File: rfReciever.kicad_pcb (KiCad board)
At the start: 4 copper layers, 22.8 x 34 mm, 34 parts, among them J1 MOLEX 1054440001, SW1 RF_RESET, SW2 RF_SLEEP, U1 TLV70130DBVR, U2 USBLC6-2SC6, U3 FT234XD-R, X1 DigiXBeeRX900Micro

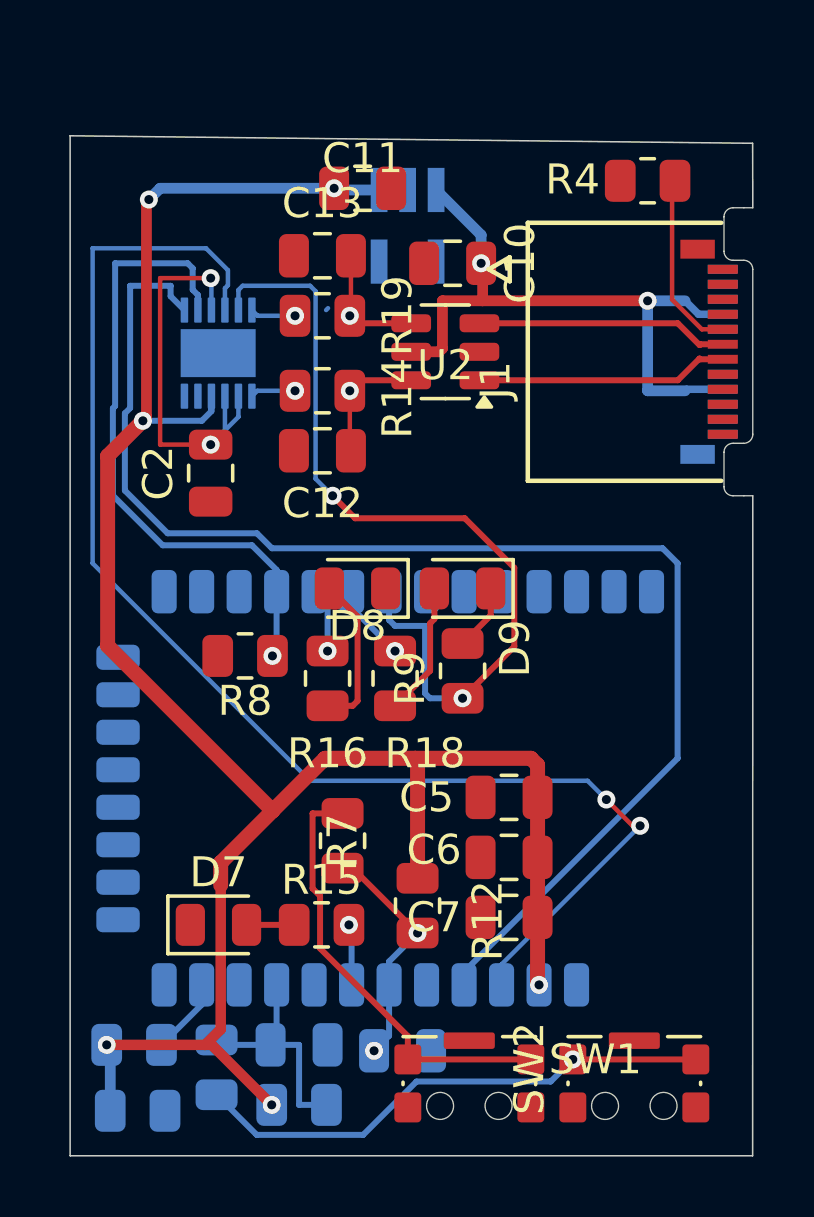
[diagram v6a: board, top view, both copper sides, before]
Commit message: added testpoints, TODO: Ground pours + ground conn
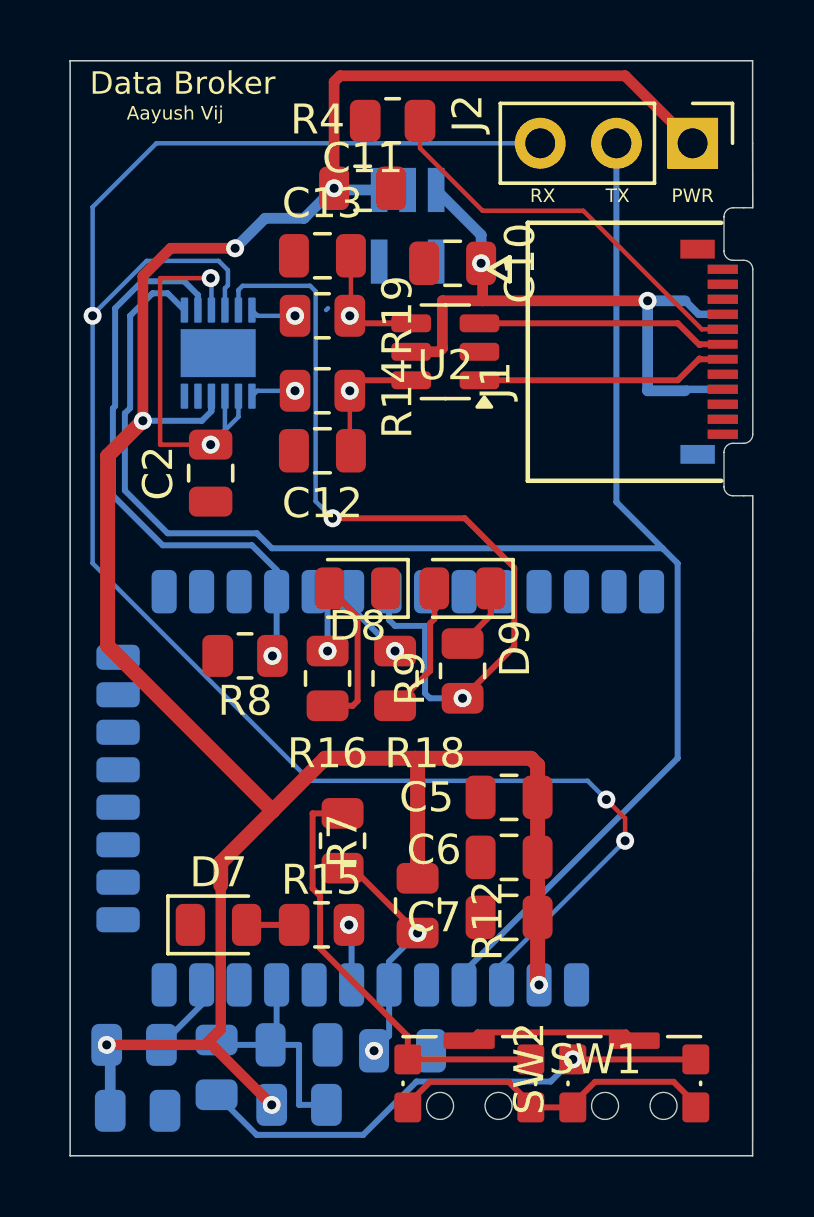
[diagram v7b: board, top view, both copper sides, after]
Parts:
- added J2: Conn_01x03, Connector_PinHeader_2.54mm:PinHeader_1x03_P2.54mm_Vertical, F.Cu at (153.8, 54.5)
- moved R4 8.73 mm to (143.8, 53.8)
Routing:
- net /RF_RXD: track 45.8 -> 63.0 mm, vias 2 -> 3
- net GND: track 2.23 -> 19.2 mm
- net +3.3V: track 72.8 -> 87.9 mm
- net /RF_TXD: track 45.7 -> 58.8 mm
- net Net-(J1-CC): track 6.46 -> 13.5 mm
- net /UART_RTS: track 21.3 -> 19.5 mm
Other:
- board size 22.8 x 34 mm -> 22.8 x 36.5 mm
- board text added: "Aayush Vij"
- board text added: "Data Broker"
- board text added: "PWR"
- board text added: "RX"
- board text added: "TX"

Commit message: ground pours + ground vias
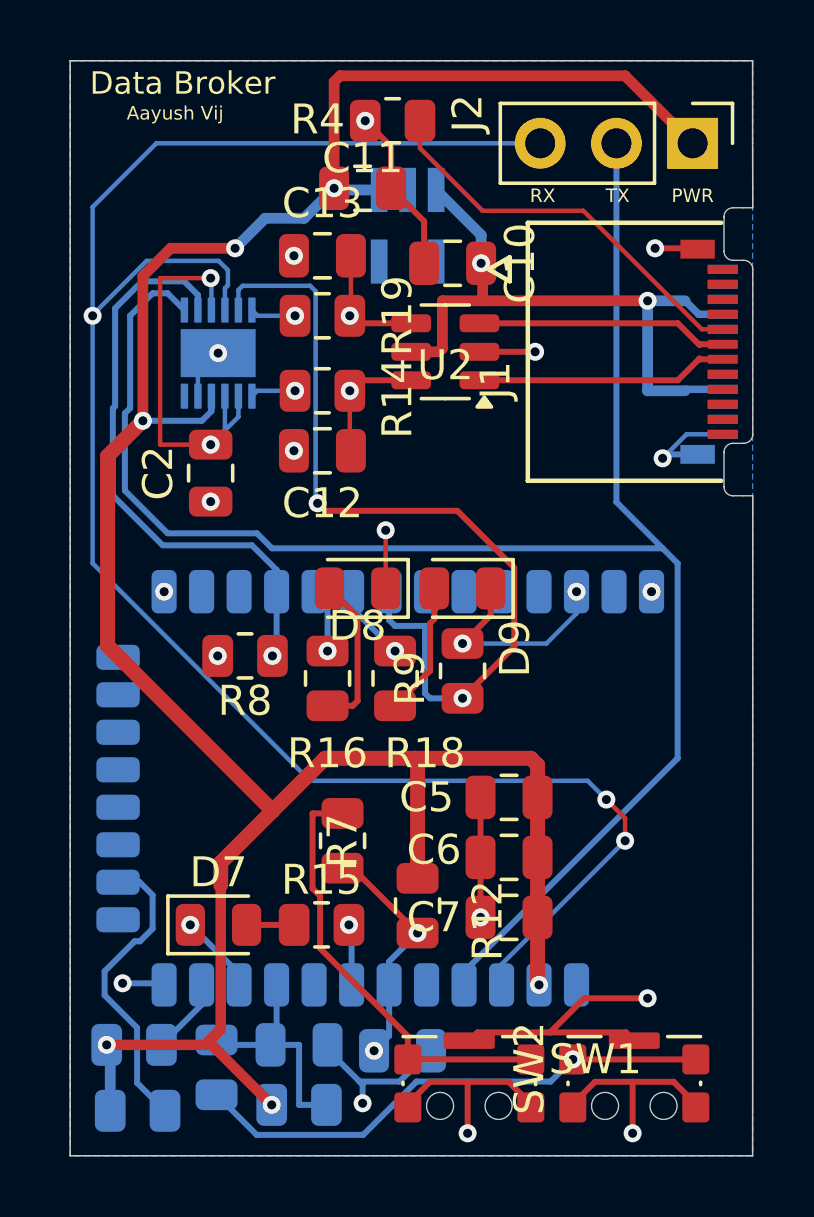
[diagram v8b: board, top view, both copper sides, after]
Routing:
- net GND: track 19.2 -> 59.9 mm, vias 0 -> 21
- net Net-(X1-SPI_N_SSEL/DIO17): track 0.00 -> 10.1 mm
- added copper zone on B.Cu, net GND
- added copper zone on In1.Cu, net GND
- added copper zone on In2.Cu, net GND
